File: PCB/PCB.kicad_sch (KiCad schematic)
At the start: 92 parts, among them J1 Conn_01x02, J2 Conn_01x02, U1 ADXL345, U2 Seeed Studio XIAO nRF52840, U3 ADXL345, U4 Seeed Studio XIAO nRF52840

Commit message: bulk
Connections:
- net +3.3V: now also R1.1, R2.1, U1.7 (~{CS})
- net +3.3VA: now also R3.1, R4.1, U3.7 (~{CS})
- net GND: now also U1.12 (SDO/ALT_ADDRESS); no longer U1.7 (~{CS})
- net GND1: now also U3.12 (SDO/ALT_ADDRESS); no longer U3.7 (~{CS})
- net SCL: now also R1.2, U2.6 (P0.05_A5_D5_SCL); no longer R1.1
- net SCLB: now also R3.2, U4.6 (P0.05_A5_D5_SCL); no longer R4.1
- net SDA: now also R2.2, U2.5 (P0.04_A4_D4_SDA); no longer R2.1
- net SDAB: now also R4.2, U4.5 (P0.04_A4_D4_SDA); no longer R3.1
- no-connect marks 6 -> 4
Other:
- moved on the sheet: R1, R2

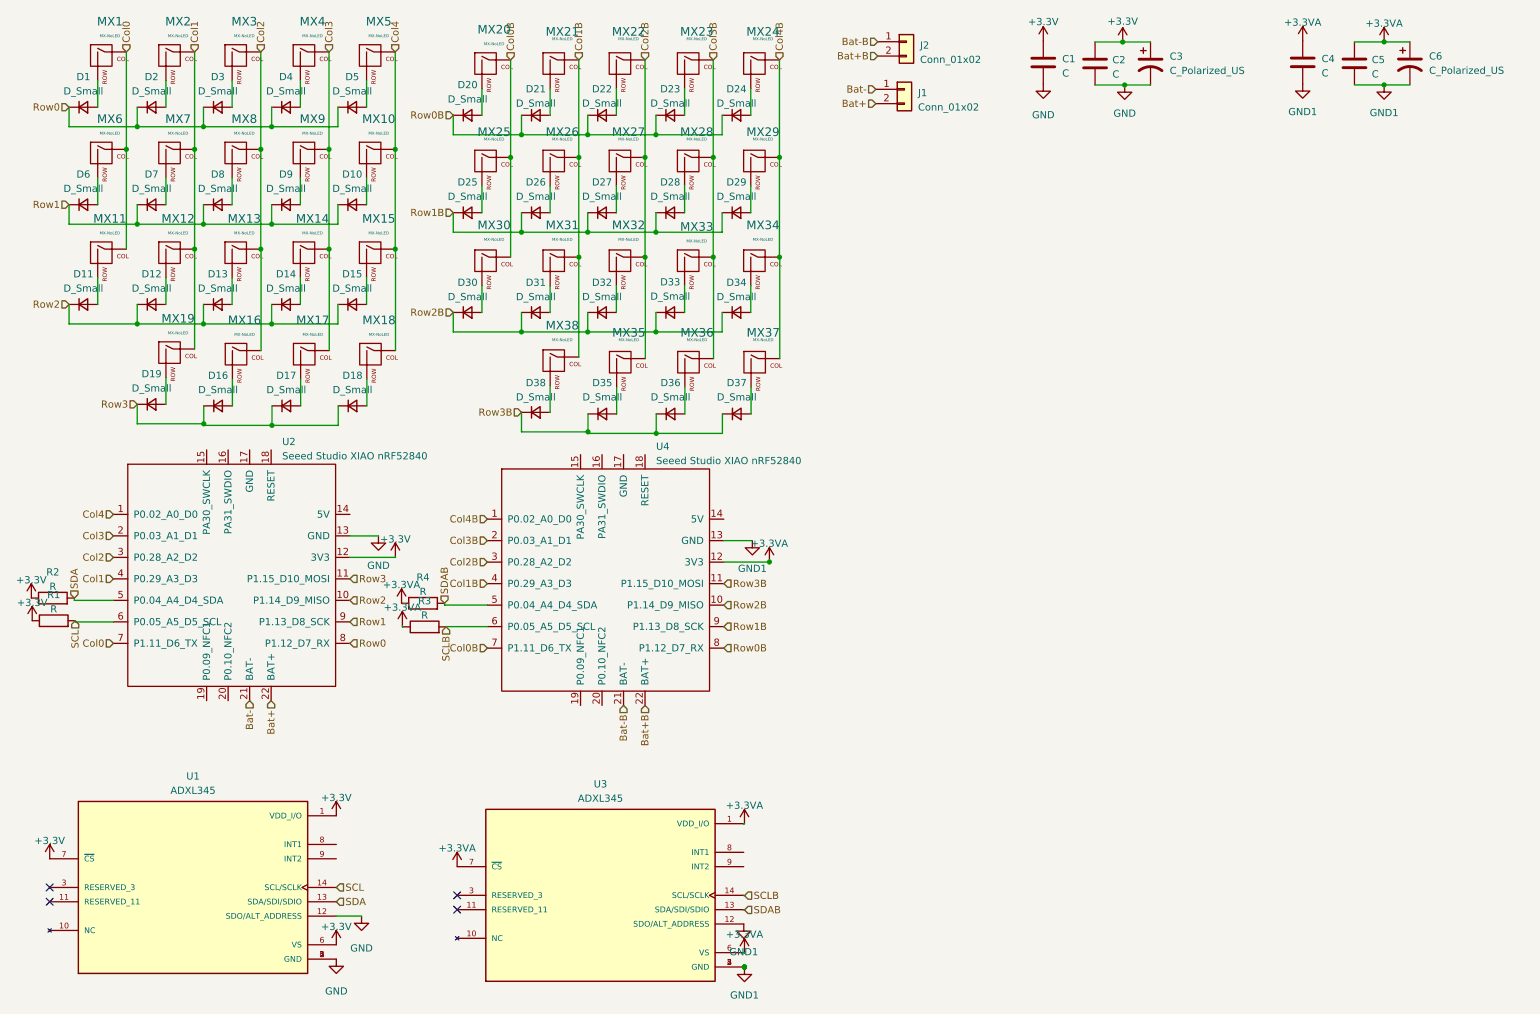
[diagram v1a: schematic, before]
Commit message: 1.2 changes for pass through charging and mounting
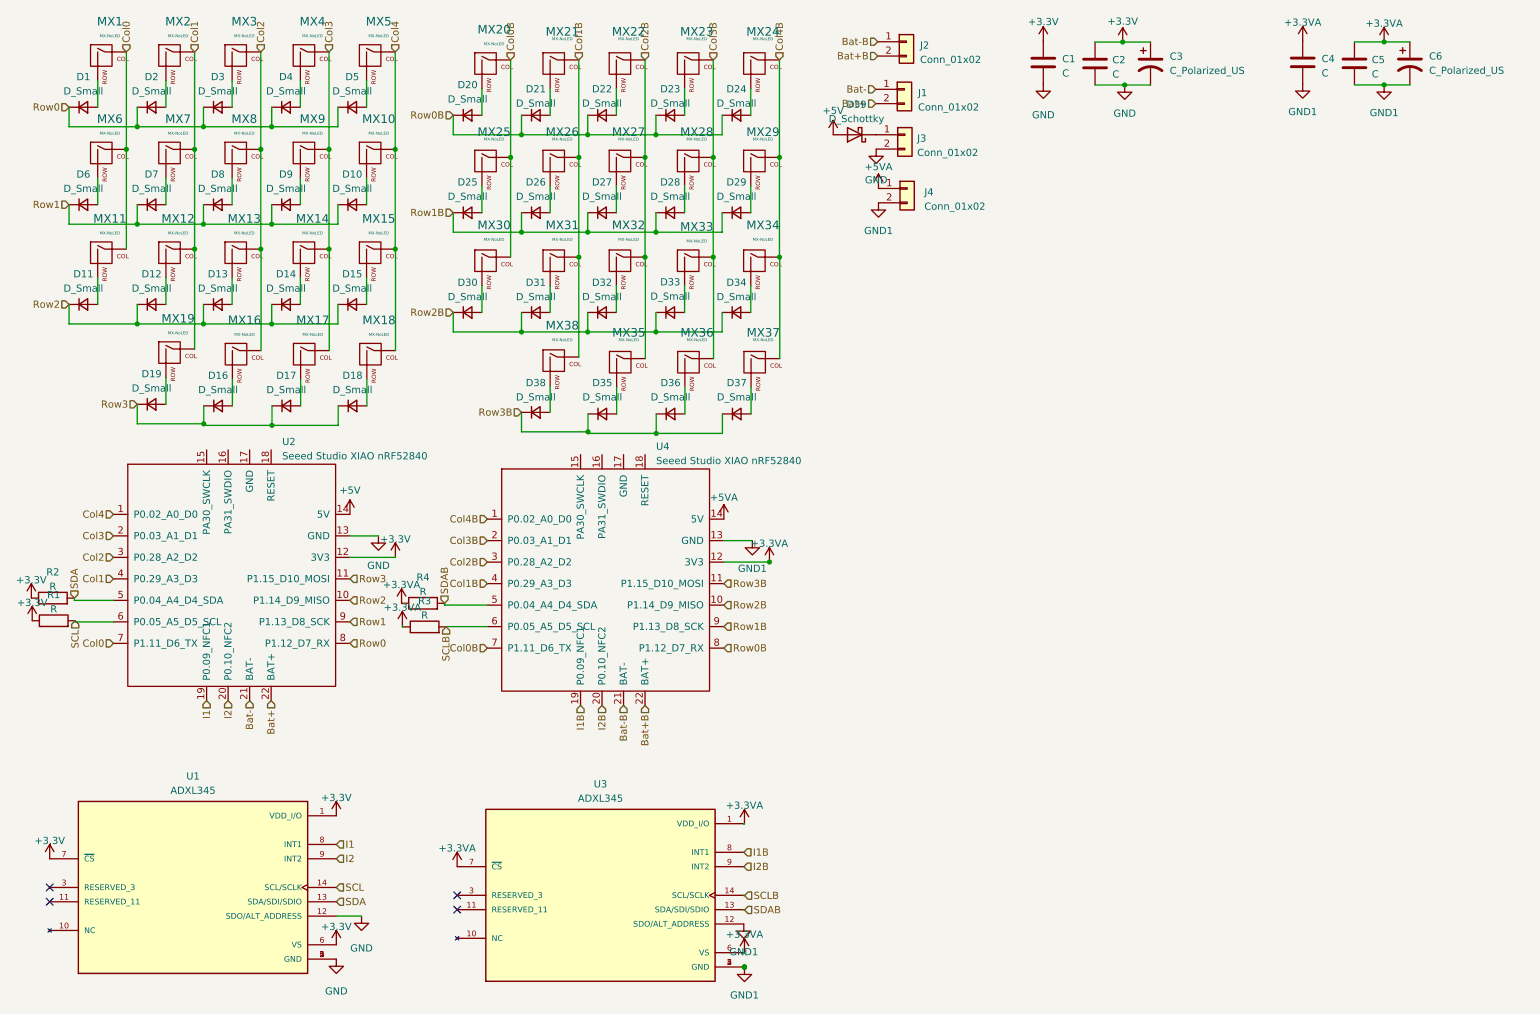
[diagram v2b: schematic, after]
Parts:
- added D39: D_Schottky, Diode_SMD:D_SOD-123, symbol Device:D_Schottky
- added J3, J4: Conn_01x02, Connector_PinHeader_2.54mm:PinHeader_1x02_P2.54mm_Vertical, symbol Connector_Generic:Conn_01x02
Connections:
- net GND: now also J3.2 (Pin_2)
- net GND1: now also J4.2 (Pin_2)
- net +5V: now reaches U2.14 (5V)
- net +5V: now also D39.2 (A)
- net I1: now reaches U2.19 (P0.09_NFC1)
- net I1: now also U1.8 (INT1)
- net I2: now reaches U2.20 (P0.10_NFC2)
- net I2: now also U1.9 (INT2)
- net I1B: now reaches U3.8 (INT1)
- net I1B: now also U4.19 (P0.09_NFC1)
- net I2B: now reaches U3.9 (INT2)
- net I2B: now also U4.20 (P0.10_NFC2)
- net +5VA: now reaches U4.14 (5V)
- net +5VA: now also J4.1 (Pin_1)
- new net: D39.1 (K), J3.1 (Pin_1)
